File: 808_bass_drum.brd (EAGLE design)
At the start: 100 x 80 mm, 56 parts, among them IC1 TL072P, Q1 bc546, Q2 bc556, Q3 bc546, Q4 bc546, Q5 bc546, Q6 bc546

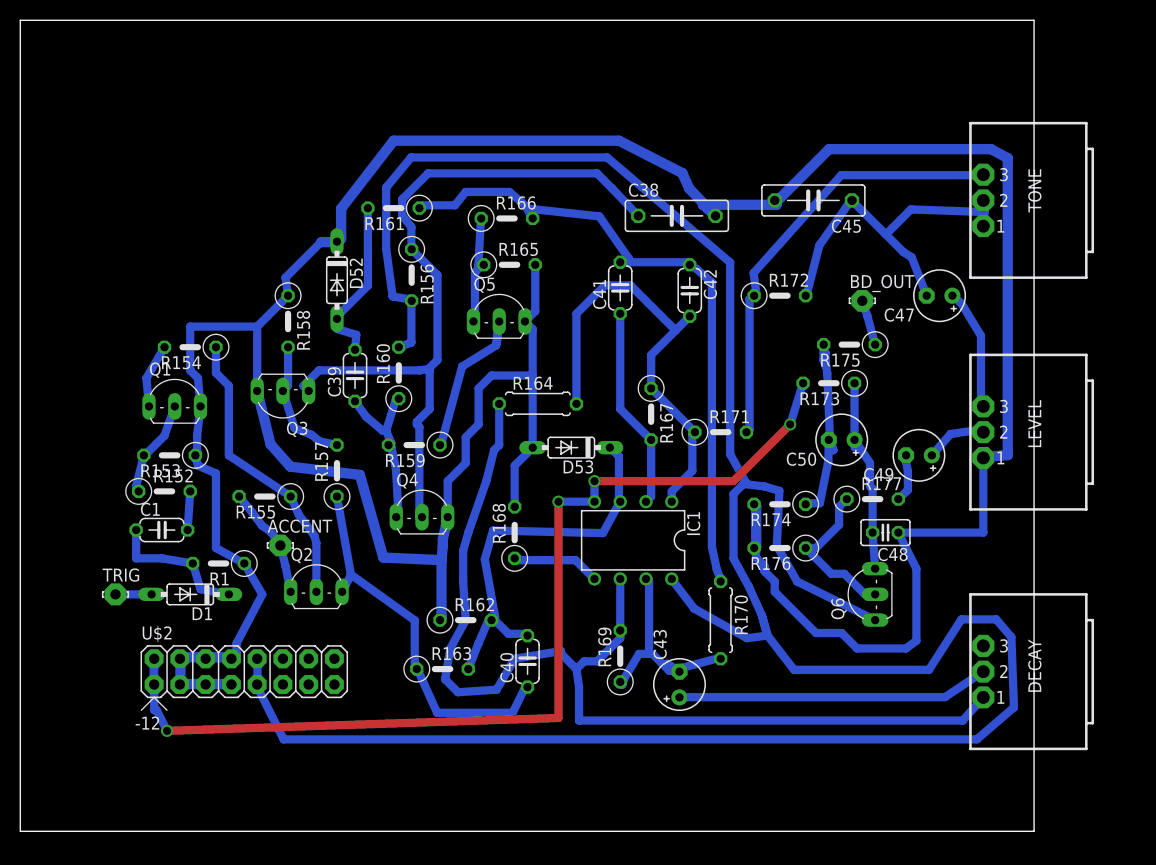
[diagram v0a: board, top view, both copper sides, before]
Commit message: updating parts and conventions
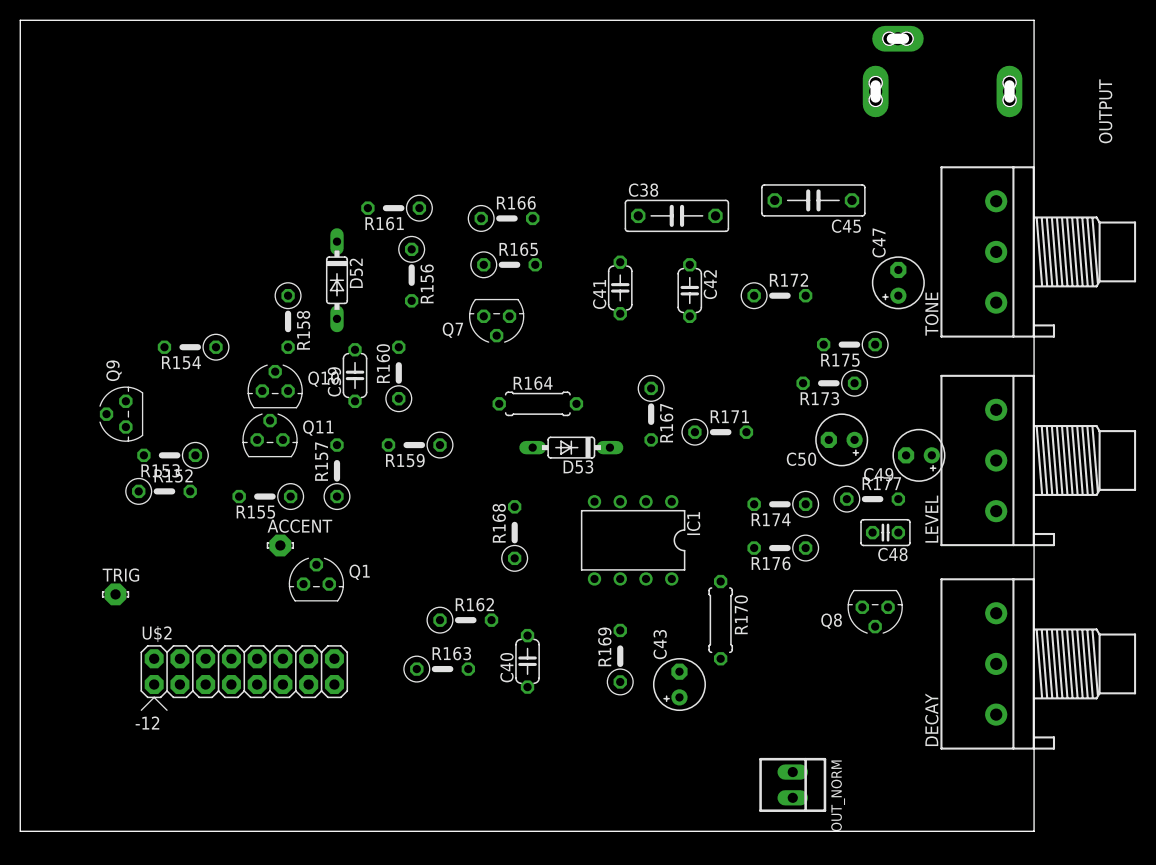
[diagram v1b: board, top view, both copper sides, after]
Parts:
- removed BD_OUT: LSP10, solpad:LSP10
- removed C1: 0.1, TR808clone:C050-024X044
- removed D1: 1N4148DO35-7, TR808clone:DO35-7
- removed Q2: bc556, transistor:TO92-EBC
- removed Q3, Q4, Q5, Q6: bc546, transistor:TO92-CBE
- removed R1: 100K, TR808clone:0207/5V
- added OUTPUT: AUDIO-JACK, erthenvar:ERTHENVAR-JACK-90DEG
- added OUT_NORM: 22-23-2021, con-molex:22-23-2021
- added Q10, Q11, Q7, Q8, Q9: 2N3904, 808_lt:TO92
- DECAY, LEVEL, TONE: device bourns:91 -> pot:3RP/1610N
- Q1: value bc546 -> 2N3906; device transistor:TO92-CBE -> 808_lt:TO92
- moved Q1 22.4 mm to (29.2, 24.4)
- moved TONE 5.24 mm to (96.3, 57.1), turned to 90 degrees
- moved C47 4.26 mm to (86.6, 54.1), turned to 90 degrees
- moved LEVEL 3.07 mm to (96.3, 36.6), turned to 90 degrees
- moved DECAY 1.48 mm to (96.3, 16.5), turned to 90 degrees
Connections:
- removed net N$3 (its old number): BD_OUT.MP, R175.1
- removed net N$5: C1.1, D1.C, R1.2
- removed net N$6: C1.2, R152.2
- new net LT_LC_OUT: OUTPUT.P$3, R175.1
- new net N$7: OUTPUT.P$2, OUT_NORM.1
- net +12V: now also Q8.1; no longer Q6.C
- net GND: now also OUTPUT.P$1, OUT_NORM.2, Q10.3, Q11.3, Q7.3, Q9.3; no longer Q1.E, Q3.E, Q4.E, Q5.E, R1.1
- net N$162: now also Q10.1, Q11.2; no longer Q3.C, Q4.B
- net N$164: now also Q1.2; no longer Q2.B
- net N$168: now also Q7.1; no longer Q5.C
- net N$169: now also Q10.2; no longer Q3.B
- net N$188: now also Q9.1; no longer Q1.C
- net N$190: now also Q11.1; no longer Q4.C
- net N$191: now also Q1.1; no longer Q2.C
- net N$193: now also Q7.2; no longer Q5.B
- net N$203: now also Q8.2; no longer Q6.B
- net N$204: now also Q8.3; no longer Q6.E
- net N$217: now also Q9.2; no longer Q1.B
- net N$4: now also R152.2, U$2.15, U$2.16; no longer D1.A
- net TRIG: now also Q1.3, U$2.13, U$2.14; no longer Q2.E
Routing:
- net GND: track 326.9 -> 0.00 mm
- net +12V: track 249.2 -> 0.00 mm
- net N$1: track 101.9 -> 0.00 mm
- net -12V: track 101.6 -> 0.00 mm, vias 4 -> 0
- net N$162: track 73.9 -> 0.00 mm
- net N$195: track 67.1 -> 0.00 mm
- net N$197: track 44.3 -> 0.00 mm
- net N$199: track 43.2 -> 0.00 mm
- net N$192: track 39.3 -> 0.00 mm
- net N$191: track 38.1 -> 0.00 mm
- net N$198: track 36.3 -> 0.00 mm
- net N$208: track 31.3 -> 0.00 mm
- net N$164: track 28.6 -> 0.00 mm
- net N$202: track 23.5 -> 0.00 mm
- net N$205: track 21.9 -> 0.00 mm
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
